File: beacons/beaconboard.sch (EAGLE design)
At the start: 33 parts, among them IC1 7805TV, Q1 2N3904

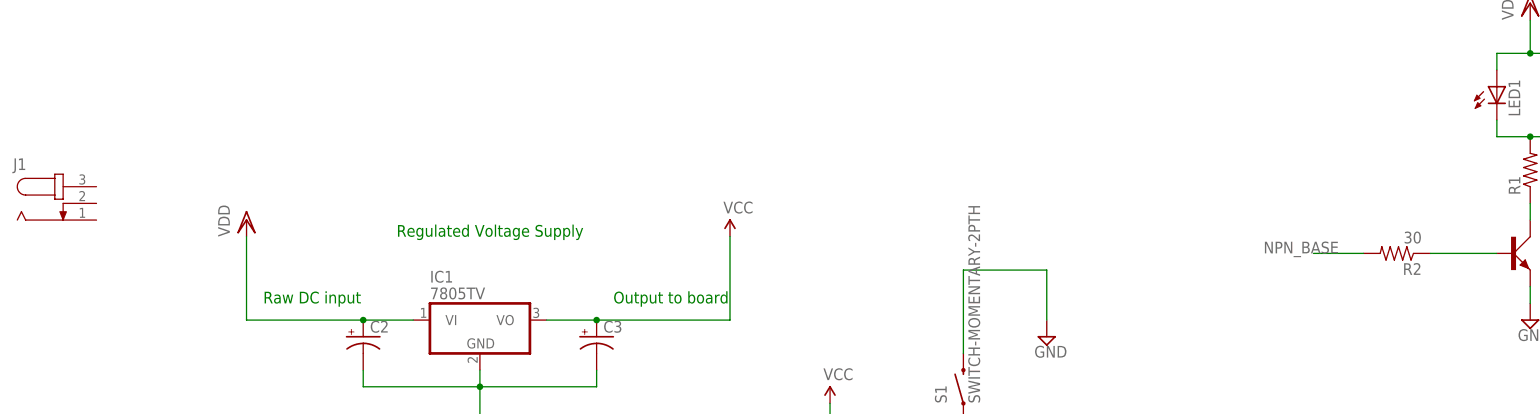
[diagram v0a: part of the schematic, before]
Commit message: added DC jack; fixed NPN base resistor val
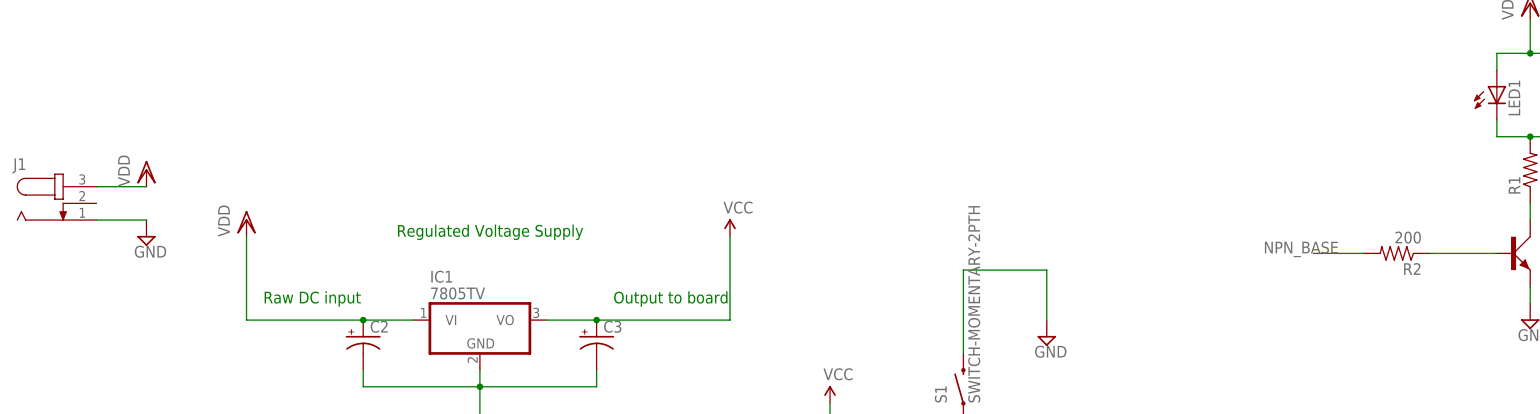
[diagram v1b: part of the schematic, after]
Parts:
- R2: value 30 -> 200
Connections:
- net GND: now also J1.1
- net VDD: now also J1.3
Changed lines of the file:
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@@
 <part name="SUPPLY4" library="supply2" deviceset="GND" device=""/>
 <part name="R1" library="SparkFun-Resistors" deviceset="RESISTOR" device="PTH-1/4W" value="30"/>
-<part name="R2" library="SparkFun-Resistors" deviceset="RESISTOR" device="PTH-1/4W" value="30"/>
+<part name="R2" library="SparkFun-Resistors" deviceset="RESISTOR" device="PTH-1/4W" value="200"/>
 <part name="VDD2" library="supply1" deviceset="VDD" device=""/>
 <part name="R3" library="SparkFun-Resistors" deviceset="RESISTOR" device="PTH-1/4W" value="200"/>
@@
 <part name="V_OUT6" library="SparkFun-Aesthetics" deviceset="VCC" device=""/>
 <part name="R11" library="SparkFun-Resistors" deviceset="RESISTOR" device="PTH-1/4W" value="200"/>
+<part name="VDD3" library="supply1" deviceset="VDD" device=""/>
+<part name="SUPPLY12" library="supply2" deviceset="GND" device=""/>
 </parts>
 <sheets>
@@
 <instance part="V_OUT6" gate="1" x="35.56" y="0"/>
 <instance part="R11" gate="G$1" x="25.4" y="-2.54" rot="R180"/>
+<instance part="VDD3" gate="G$1" x="-20.32" y="116.84"/>
+<instance part="SUPPLY12" gate="GND" x="-20.32" y="106.68"/>
 </instances>
 <busses>
@@
 <wire x1="195.58" y1="134.62" x2="195.58" y2="132.08" width="0.1524" layer="91"/>
 <junction x="190.5" y="134.62"/>
+</segment>
+<segment>
+<pinref part="J1" gate="G$1" pin="3"/>
+<pinref part="VDD3" gate="G$1" pin="VDD"/>
+<wire x1="-20.32" y1="114.3" x2="-27.94" y2="114.3" width="0.1524" layer="91"/>
 </segment>
 </net>
@@
 <wire x1="190.5" y1="96.52" x2="190.5" y2="99.06" width="0.1524" layer="91"/>
 </segment>
+<segment>
+<pinref part="J1" gate="G$1" pin="1"/>
+<pinref part="SUPPLY12" gate="GND" pin="GND"/>
+<wire x1="-20.32" y1="109.22" x2="-27.94" y2="109.22" width="0.1524" layer="91"/>
+</segment>
 </net>
